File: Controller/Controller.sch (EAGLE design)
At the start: 41 parts, among them SW1 SWITCH-PTS-810, U1 ATSAMD21E18A-AU, U2 MIC5205-3.3YM5 TR, X1 CRYSTAL-AB26TRQ-32.768K

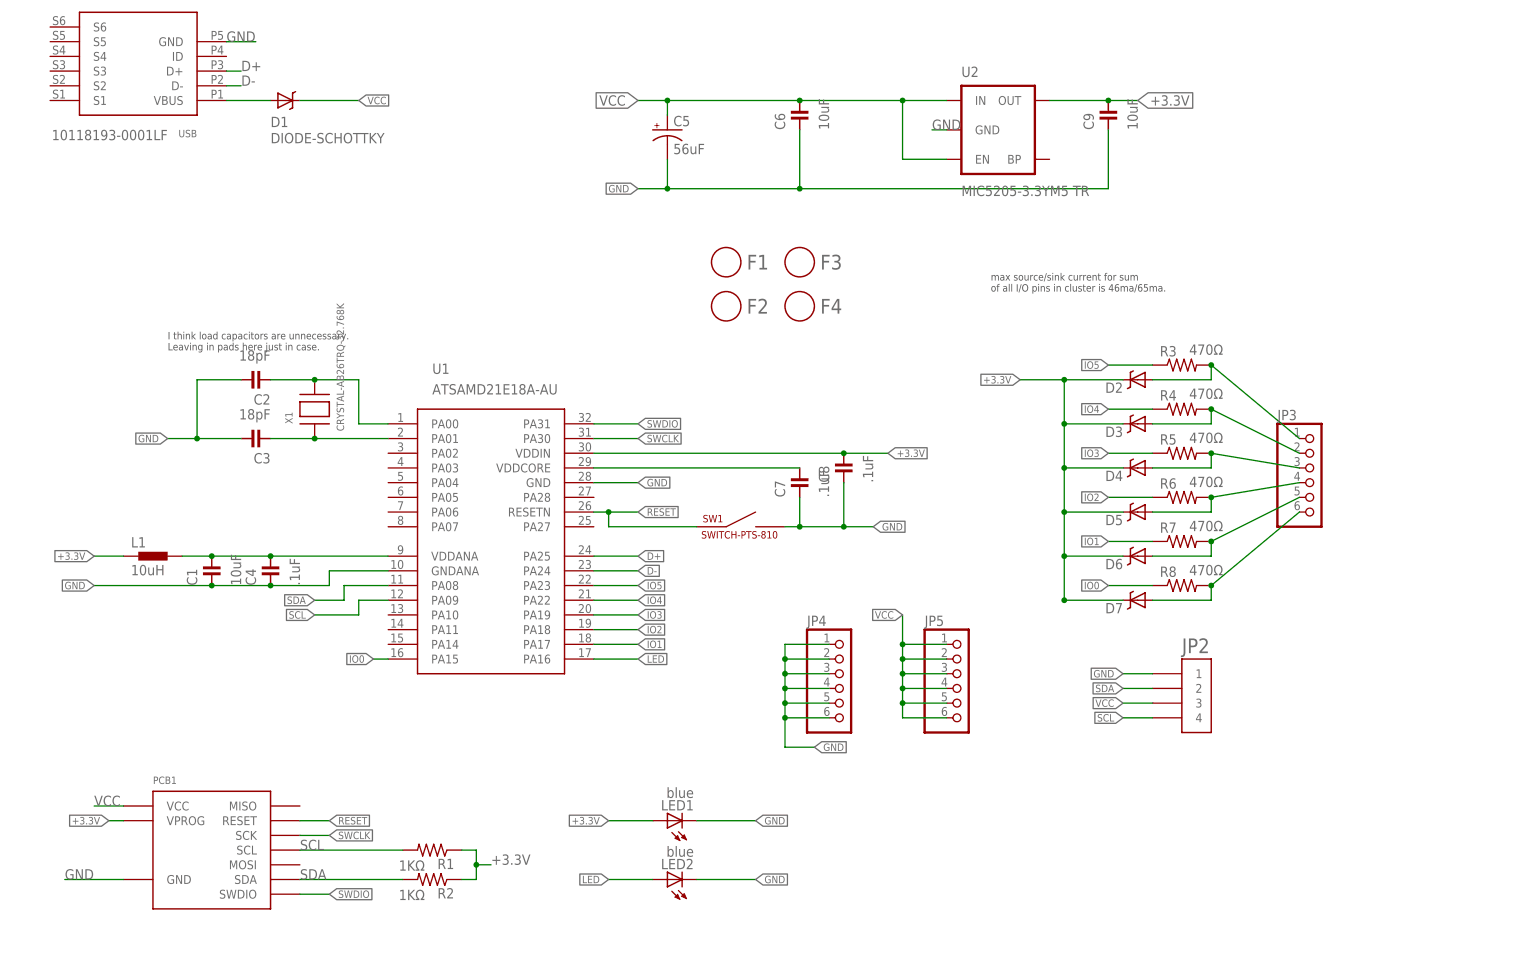
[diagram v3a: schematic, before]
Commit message: Fixed bad clamp diode wiring and added a reverse protection diode
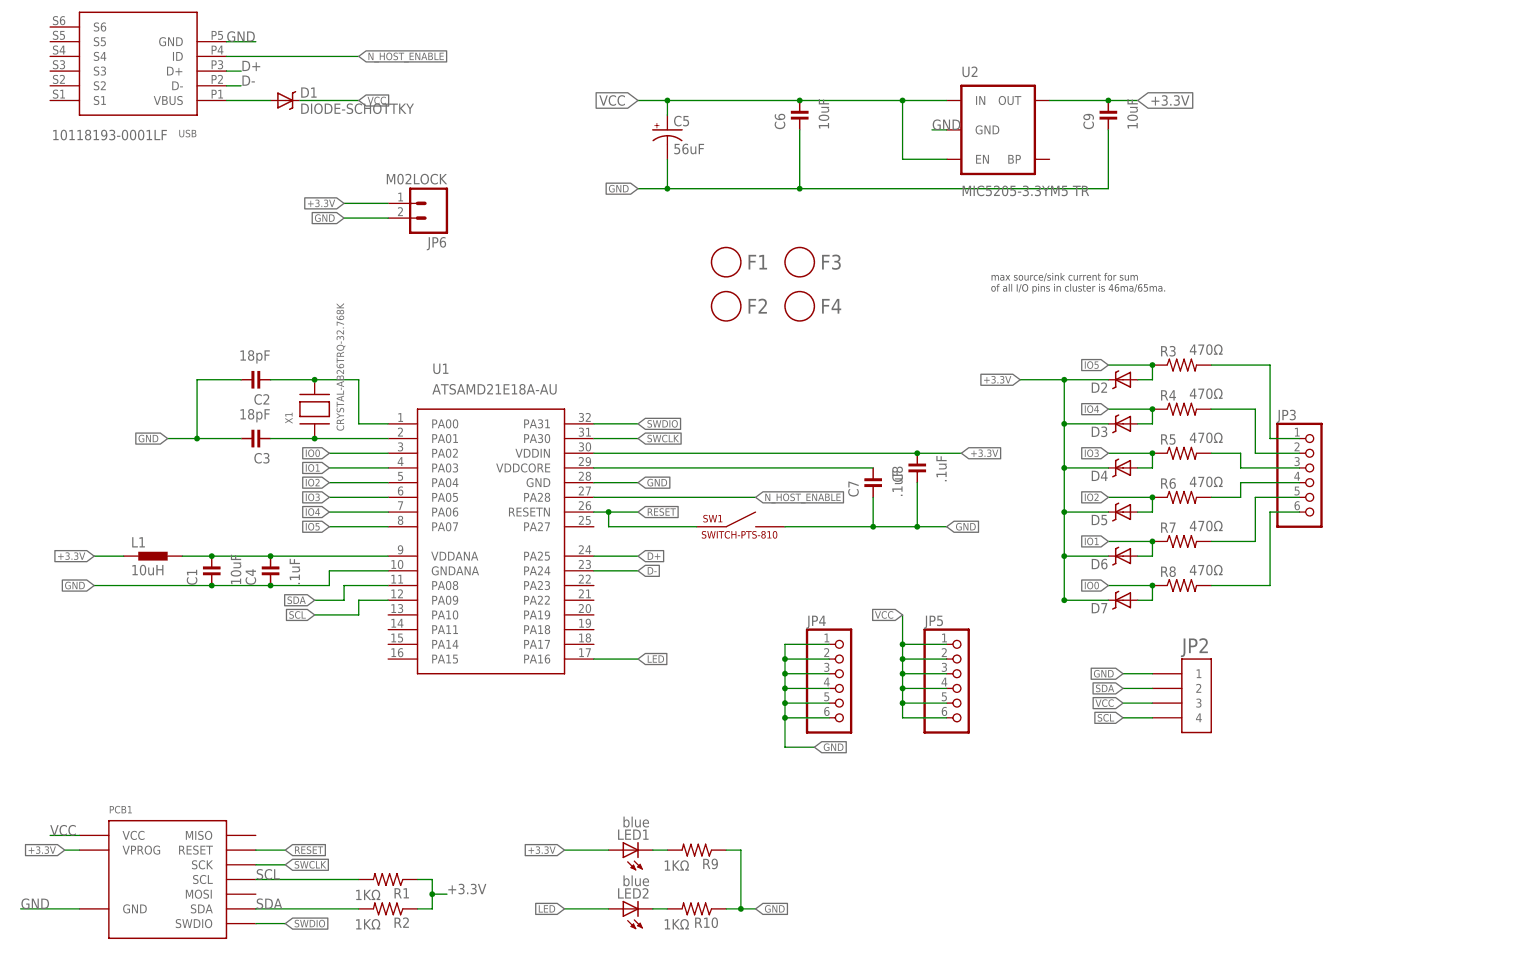
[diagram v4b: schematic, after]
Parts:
- added JP6: M02LOCK, SparkFun-Connectors:M02LOCK
- added R10, R9: 1KΩ, Modulo:RESISTOR-1KΩ
- C2, C3: BOM EXCLUDE -> (none)
- D2, D3, D4, D5, D6, D7: PARTNUM CUS520,H3F -> RB751V40
- JP3, JP4, JP5: PARTNUM PREC006SAAN-RC -> M20-9990646
- LED1: PARTNUM (none) -> LTST-C171KRKT
- U1: PARTNUM ATSAMD21E18A-AU -> ATSAMD21E18A-AUT
- U2: PARTNUM MIC5205-3.3YM5 -> MIC5205-3.3YM5 TR
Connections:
- new net N$1: LED1.C, R9.2
- new net N$4: LED2.C, R10.2
- new net N_HOST_ENABLE: JP1.ID, U1.PA28
- net +3.3V: now also JP6.1
- net GND: now also JP6.2, R10.1, R9.1; no longer LED1.C, LED2.C
- net IO0: now also D7.A, U1.PA02; no longer U1.PA15
- net IO1: now also D6.A, U1.PA03; no longer U1.PA17
- net IO2: now also D5.A, U1.PA04; no longer U1.PA18
- net IO3: now also D4.A, U1.PA05; no longer U1.PA19
- net IO4: now also D3.A, U1.PA06; no longer U1.PA22
- net IO5: now also D2.A, U1.PA07; no longer U1.PA23
- net N$13: no longer D3.A
- net N$17: no longer D4.A
- net N$18: no longer D5.A
- net N$19: no longer D6.A
- net N$2: no longer D2.A
- net N$20: no longer D7.A
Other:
- note removed: "I think load capacitors are unnecessary. Leaving in pads here just in case."
- moved on the sheet: C7, C8, D2, D3, D4, D5, D6, D7, LED1, LED2, PCB1, R1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
